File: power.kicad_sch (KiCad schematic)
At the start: 29 parts, among them U2 NCP691MN33T2G, U4 AP63301WU-7, U5 AP63301WU-7

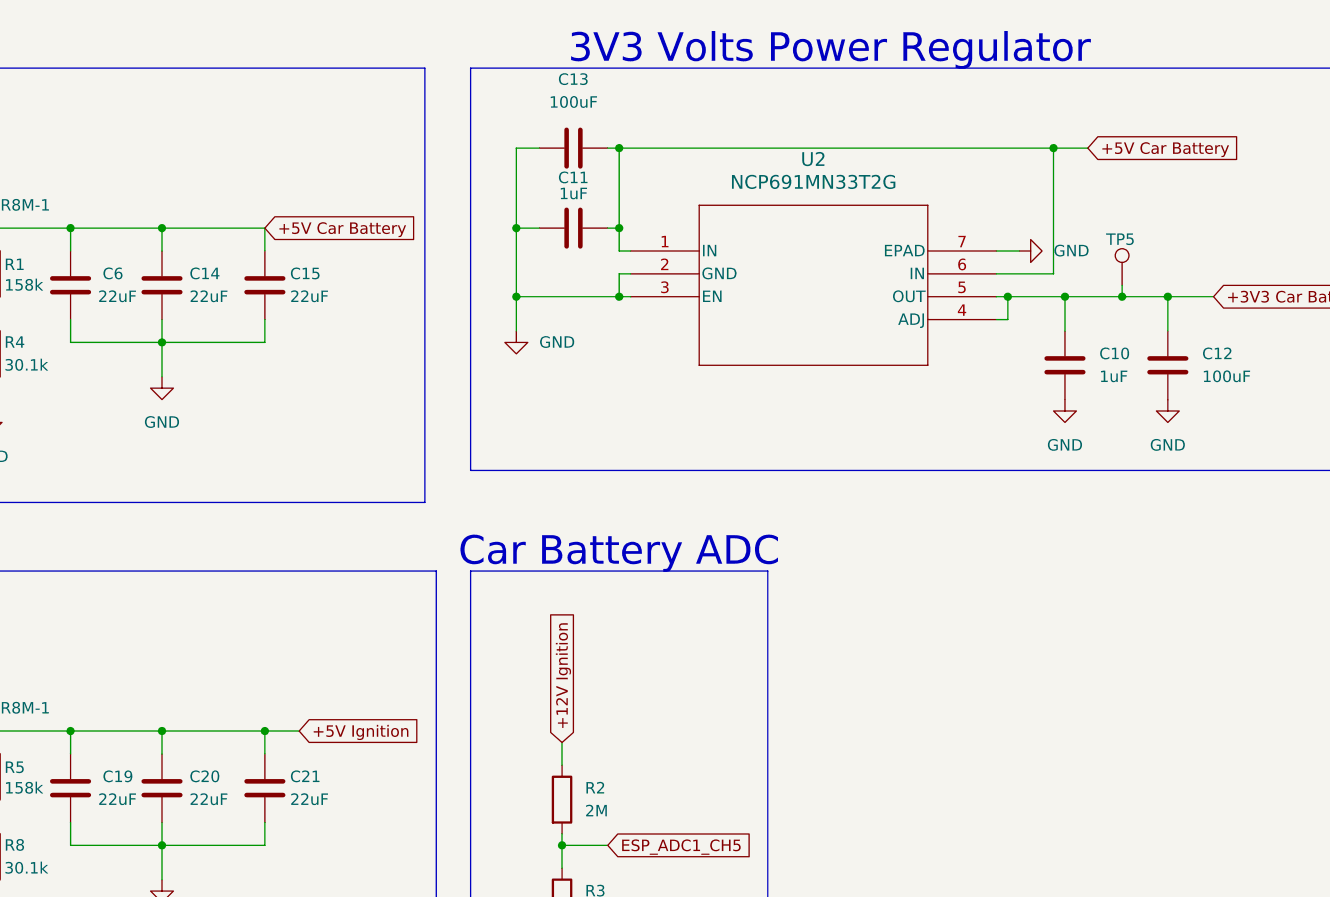
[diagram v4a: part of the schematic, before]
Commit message: added 3D models; light touch-ups
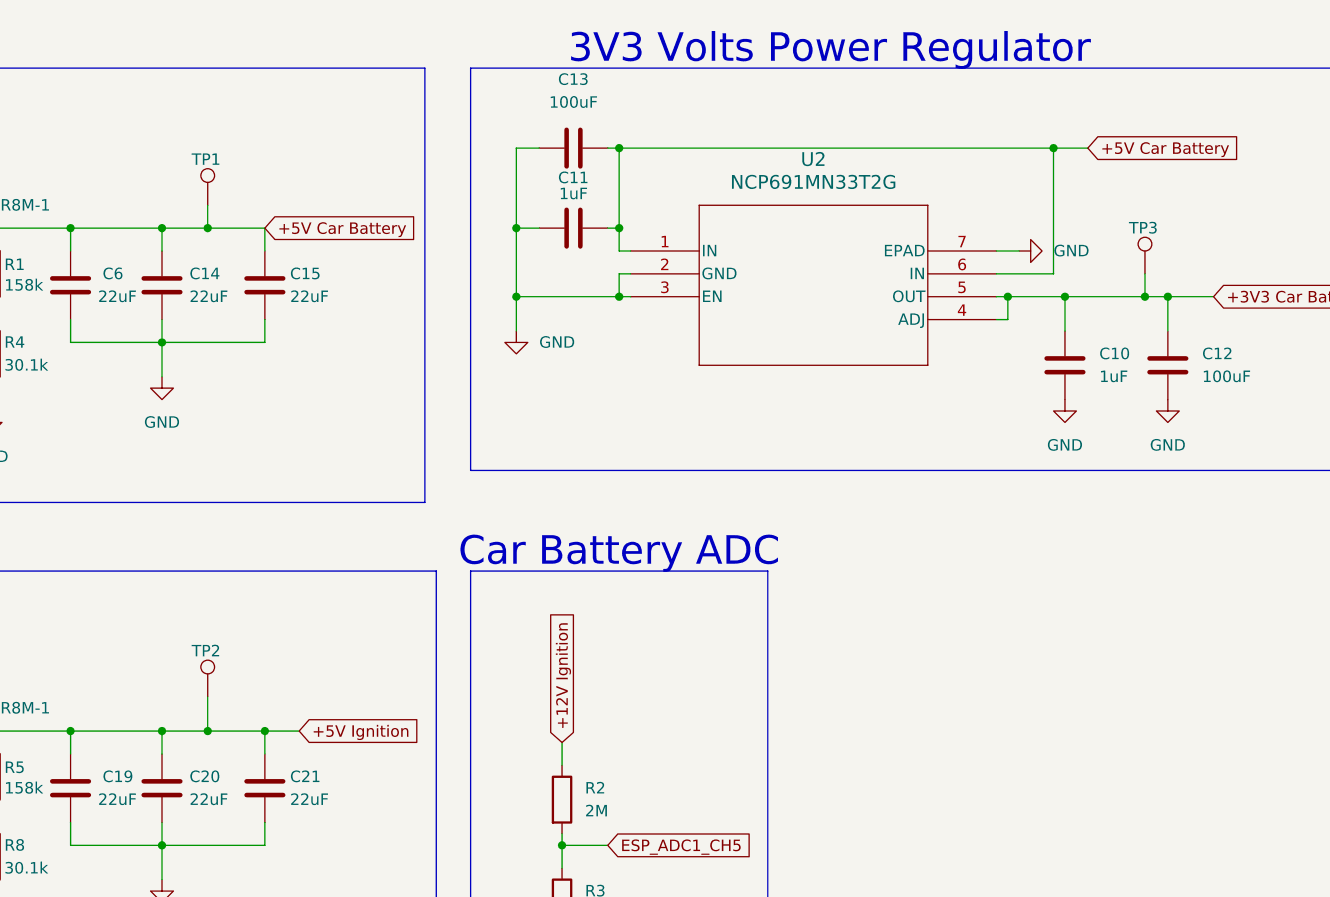
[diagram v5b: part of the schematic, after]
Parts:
- removed TP5: TestPoint, TestPoint:TestPoint_Pad_D1.0mm, symbol Connector:TestPoint
- added TP1, TP2, TP3: TestPoint, TestPoint:TestPoint_Pad_D1.0mm, symbol Connector:TestPoint
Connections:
- net +3V3 Car Battery: now also TP3.1
- net +5V Car Battery: now also TP1.1
- net +5V Ignition: now also TP2.1
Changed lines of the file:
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@@
 	)
 	(junction
+		(at 143.51 90.17)
+		(diameter 0)
+		(color 0 0 0 0)
+	)
+	(junction
 		(at 53.34 25.4)
 		(diameter 0)
@@
 	)
 	(junction
-		(at 245.11 41.91)
+		(at 247.65 41.91)
 		(diameter 0)
 		(color 0 0 0 0)
@@
 	)
 	(junction
+		(at 143.51 34.29)
+		(diameter 0)
+		(color 0 0 0 0)
+	)
+	(junction
 		(at 96.52 34.29)
 		(diameter 0)
@@
 	(wire
 		(pts
-			(xy 245.11 41.91) (xy 250.19 41.91)
+			(xy 238.76 41.91) (xy 247.65 41.91)
 		)
 		(stroke
@@
 	(wire
 		(pts
-			(xy 238.76 41.91) (xy 245.11 41.91)
+			(xy 119.38 99.06) (xy 119.38 100.33)
 		)
 		(stroke
@@
 	(wire
 		(pts
-			(xy 119.38 99.06) (xy 119.38 100.33)
+			(xy 53.34 81.28) (xy 43.18 81.28)
 		)
 		(stroke
@@
 	(wire
 		(pts
-			(xy 53.34 81.28) (xy 43.18 81.28)
+			(xy 149.86 44.45) (xy 149.86 46.99)
 		)
 		(stroke
@@
 	(wire
 		(pts
-			(xy 149.86 44.45) (xy 149.86 46.99)
+			(xy 231.14 44.45) (xy 232.41 44.45)
 		)
 		(stroke
@@
 	(wire
 		(pts
-			(xy 231.14 44.45) (xy 232.41 44.45)
+			(xy 247.65 41.91) (xy 250.19 41.91)
 		)
 		(stroke
@@
 	(wire
 		(pts
-			(xy 149.86 34.29) (xy 138.43 34.29)
+			(xy 149.86 34.29) (xy 143.51 34.29)
 		)
 		(stroke
@@
 	(wire
 		(pts
+			(xy 143.51 90.17) (xy 138.43 90.17)
+		)
+		(stroke
+			(width 0)
+			(type default)
+		)
+	)
+	(wire
+		(pts
 			(xy 232.41 44.45) (xy 232.41 41.91)
 		)
@@
 	(wire
 		(pts
-			(xy 149.86 90.17) (xy 138.43 90.17)
+			(xy 149.86 90.17) (xy 143.51 90.17)
 		)
 		(stroke
@@
 	(wire
 		(pts
+			(xy 143.51 86.36) (xy 143.51 90.17)
+		)
+		(stroke
+			(width 0)
+			(type default)
+		)
+	)
+	(wire
+		(pts
 			(xy 189.23 25.4) (xy 189.23 34.29)
 		)
@@
 	(wire
 		(pts
+			(xy 247.65 39.37) (xy 247.65 41.91)
+		)
+		(stroke
+			(width 0)
+			(type default)
+		)
+	)
+	(wire
+		(pts
 			(xy 138.43 102.87) (xy 149.86 102.87)
 		)
@@
 	(wire
 		(pts
-			(xy 245.11 40.64) (xy 245.11 41.91)
+			(xy 143.51 34.29) (xy 138.43 34.29)
+		)
+		(stroke
+			(width 0)
+			(type default)
+		)
+	)
+	(wire
+		(pts
+			(xy 143.51 31.75) (xy 143.51 34.29)
 		)
 		(stroke
@@
 	)
 	(symbol
-		(lib_id "Connector:TestPoint")
-		(at 245.11 40.64 0)
-		(unit 1)
-		(exclude_from_sim no)
-		(in_bom yes)
-		(on_board yes)
-		(dnp no)
-		(property "Reference" "TP5"
-			(at 243.332 35.56 0)
-			(effects
-				(font
-					(size 1.27 1.27)
-				)
-				(justify left)
-			)
-		)
-		(property "Value" "TestPoint"
-			(at 242.316 35.306 0)
-			(effects
-				(font
-					(size 1.27 1.27)
-				)
-				(justify left)
-				(hide yes)
-			)
-		)
-		(property "Footprint" "TestPoint:TestPoint_Pad_D1.0mm"
-			(at 250.19 40.64 0)
-			(effects
-				(font
-					(size 1.27 1.27)
-				)
-				(hide yes)
-			)
-		)
-		(property "Datasheet" "~"
-			(at 250.19 40.64 0)
-			(effects
-				(font
-					(size 1.27 1.27)
-				)
-				(hide yes)
-			)
-		)
-		(property "Description" "test point"
-			(at 245.11 40.64 0)
-			(effects
-				(font
-					(size 1.27 1.27)
-				)
-				(hide yes)
-			)
-		)
-		(pin "1"
-		)
-		(instances
-			(project "power"
-				(path "/0794a8bf-8b4d-4965-84ee-8314ec5cc547"
-					(reference "TP?")
-					(unit 1)
-				)
-			)
-			(project "main"
-				(path "/3ec17d1d-183f-42c7-9d9d-808fb8c0b5df/d298b733-9a46-47ce-8c62-0344f0cec928"
-					(reference "TP5")
-					(unit 1)
-				)
-			)
-		)
-	)
-	(symbol
 		(lib_id "power:GND")
 		(at 48.26 99.06 0)
@@
 	)
 	(symbol
+		(lib_id "Connector:TestPoint")
+		(at 143.51 31.75 0)
+		(unit 1)
+		(exclude_from_sim no)
+		(in_bom yes)
+		(on_board yes)
+		(dnp no)
+		(property "Reference" "TP1"
+			(at 141.732 26.67 0)
+			(effects
+				(font
+					(size 1.27 1.27)
+				)
+				(justify left)
+			)
+		)
+		(property "Value" "TestPoint"
+			(at 140.716 26.416 0)
+			(effects
+				(font
+					(size 1.27 1.27)
+				)
+				(justify left)
+				(hide yes)
+			)
+		)
+		(property "Footprint" "TestPoint:TestPoint_Pad_D1.0mm"
+			(at 148.59 31.75 0)
+			(effects
+				(font
+					(size 1.27 1.27)
+				)
+				(hide yes)
+			)
+		)
+		(property "Datasheet" "~"
+			(at 148.59 31.75 0)
+			(effects
+				(font
+					(size 1.27 1.27)
+				)
+				(hide yes)
+			)
+		)
+		(property "Description" "test point"
+			(at 143.51 31.75 0)
+			(effects
+				(font
+					(size 1.27 1.27)
+				)
+				(hide yes)
+			)
+		)
+		(pin "1"
+		)
+		(instances
+			(project "main"
+				(path "/3ec17d1d-183f-42c7-9d9d-808fb8c0b5df/d298b733-9a46-47ce-8c62-0344f0cec928"
+					(reference "TP1")
+					(unit 1)
+				)
+			)
+		)
+	)
+	(symbol
 		(lib_id "Device:C")
 		(at 43.18 87.63 0)
@@
 	)
 	(symbol
+		(lib_id "Connector:TestPoint")
+		(at 143.51 86.36 0)
+		(unit 1)
+		(exclude_from_sim no)
+		(in_bom yes)
+		(on_board yes)
+		(dnp no)
+		(property "Reference" "TP2"
+			(at 141.732 81.28 0)
+			(effects
+				(font
+					(size 1.27 1.27)
+				)
+				(justify left)
+			)
+		)
+		(property "Value" "TestPoint"
+			(at 140.716 81.026 0)
+			(effects
+				(font
+					(size 1.27 1.27)
+				)
+				(justify left)
+				(hide yes)
+			)
+		)
+		(property "Footprint" "TestPoint:TestPoint_Pad_D1.0mm"
+			(at 148.59 86.36 0)
+			(effects
+				(font
+					(size 1.27 1.27)
+				)
+				(hide yes)
+			)
+		)
+		(property "Datasheet" "~"
+			(at 148.59 86.36 0)
+			(effects
+				(font
+					(size 1.27 1.27)
+				)
+				(hide yes)
+			)
+		)
+		(property "Description" "test point"
+			(at 143.51 86.36 0)
+			(effects
+				(font
+					(size 1.27 1.27)
+				)
+				(hide yes)
+			)
+		)
+		(pin "1"
+		)
+		(instances
+			(project "main"
+				(path "/3ec17d1d-183f-42c7-9d9d-808fb8c0b5df/d298b733-9a46-47ce-8c62-0344f0cec928"
+					(reference "TP2")
+					(unit 1)
+				)
+			)
+		)
+	)
+	(symbol
 		(lib_id "Device:C")
 		(at 184.15 25.4 270)
@@
 					(unit 1)
 				)
+			)
+		)
+	)
+	(symbol
+		(lib_id "Connector:TestPoint")
+		(at 247.65 39.37 0)
+		(unit 1)
+		(exclude_from_sim no)
+		(in_bom yes)
+		(on_board yes)
+		(dnp no)
+		(property "Reference" "TP3"
+			(at 245.872 34.29 0)
+			(effects
+				(font
+					(size 1.27 1.27)
+				)
+				(justify left)
+			)
+		)
+		(property "Value" "TestPoint"
+			(at 244.856 34.036 0)
+			(effects
+				(font
+					(size 1.27 1.27)
+				)
+				(justify left)
+				(hide yes)
+			)
+		)
+		(property "Footprint" "TestPoint:TestPoint_Pad_D1.0mm"
+			(at 252.73 39.37 0)
+			(effects
+				(font
+					(size 1.27 1.27)
+				)
+				(hide yes)
+			)
+		)
+		(property "Datasheet" "~"
+			(at 252.73 39.37 0)
+			(effects
+				(font
+					(size 1.27 1.27)
+				)
+				(hide yes)
+			)
+		)
+		(property "Description" "test point"
+			(at 247.65 39.37 0)
+			(effects
+				(font
+					(size 1.27 1.27)
+				)
+				(hide yes)
+			)
+		)
+		(pin "1"
+		)
+		(instances
+			(project "main"
+				(path "/3ec17d1d-183f-42c7-9d9d-808fb8c0b5df/d298b733-9a46-47ce-8c62-0344f0cec928"
+					(reference "TP3")
+					(unit 1)
+				)

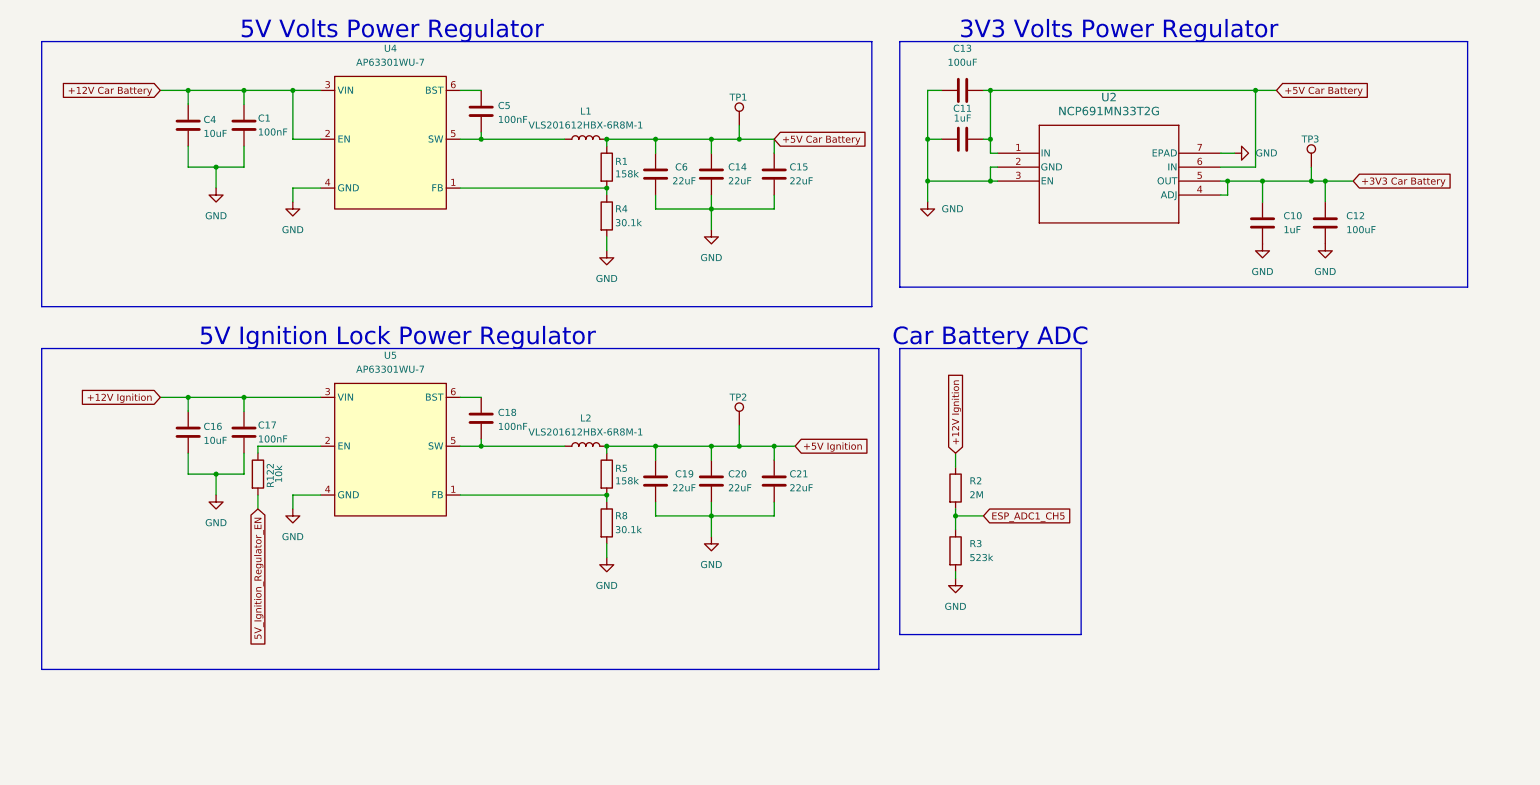
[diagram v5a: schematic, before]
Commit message: added tvs diodes, 100nF, pull-up for TSS interrupt
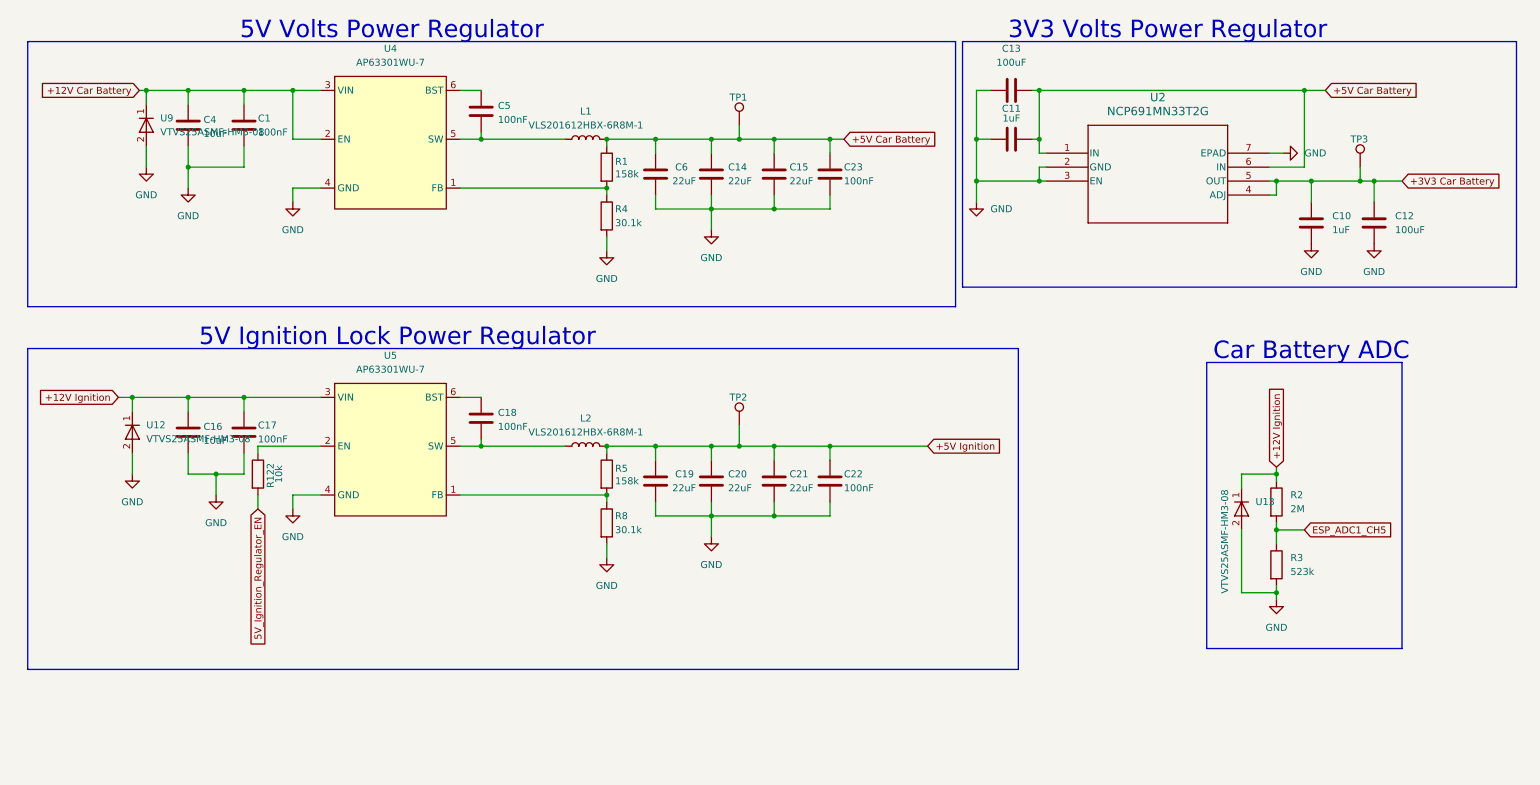
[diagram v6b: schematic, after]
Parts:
- added C22, C23: 100nF, Capacitor_SMD:C_0805_2012Metric, symbol Device:C
- added U12, U13, U9: VTVS25ASMF-HM3-08, Diode_SMD:D_SMF, symbol infotainment:VTVS25ASMF-HM3-08_
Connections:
- net +12V Car Battery: now also U9.1
- net +12V Ignition: now also U12.1, U13.1
- net +5V Car Battery: now also C23.1
- net +5V Ignition: now also C22.1
- net GND: now also C22.2, C23.2, U12.2, U13.2, U9.2
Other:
- moved on the sheet: C10, C11, C12, C13, R2, R3, TP3, U2

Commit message: Modified ADC resistors. Added bypass cap to ADC.
Removed some ground islands.
Removed lock files and added them to gitignore.
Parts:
- added C24: 100nF, Capacitor_SMD:C_0805_2012Metric, symbol Device:C
- R2: value 2M -> 90k
- R3: value 523k -> 10k
- renumbered TP3 to 3V3_B1, TP1 to 5V_B1, TP2 to 5V_I1
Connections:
- net ESP_ADC1_CH5: now also C24.1
- net GND: now also C24.2
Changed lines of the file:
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@@
 	)
 	(junction
+		(at 252.73 105.41)
+		(diameter 0)
+		(color 0 0 0 0)
+	)
+	(junction
 		(at 259.08 41.91)
 		(diameter 0)
@@
 	(wire
 		(pts
+			(xy 252.73 105.41) (xy 260.35 105.41)
+		)
+		(stroke
+			(width 0)
+			(type default)
+		)
+	)
+	(wire
+		(pts
 			(xy 196.85 25.4) (xy 198.12 25.4)
 		)
@@
 	(wire
 		(pts
+			(xy 252.73 114.3) (xy 252.73 116.84)
+		)
+		(stroke
+			(width 0)
+			(type default)
+		)
+	)
+	(wire
+		(pts
 			(xy 246.38 25.4) (xy 246.38 39.37)
 		)
@@
 	(wire
 		(pts
-			(xy 241.3 105.41) (xy 246.38 105.41)
+			(xy 241.3 105.41) (xy 252.73 105.41)
 		)
 		(stroke
@@
 	(wire
 		(pts
+			(xy 252.73 106.68) (xy 252.73 105.41)
+		)
+		(stroke
+			(width 0)
+			(type default)
+		)
+	)
+	(wire
+		(pts
 			(xy 62.23 34.29) (xy 62.23 25.4)
 		)
@@
 	(wire
 		(pts
+			(xy 252.73 116.84) (xy 241.3 116.84)
+		)
+		(stroke
+			(width 0)
+			(type default)
+		)
+	)
+	(wire
+		(pts
 			(xy 53.34 83.82) (xy 53.34 81.28)
 		)
@@
 	(global_label "ESP_ADC1_CH5"
 		(shape input)
-		(at 246.38 105.41 0)
+		(at 260.35 105.41 0)
 		(fields_autoplaced yes)
 		(effects
@@
 		)
 		(property "Intersheetrefs" "${INTERSHEET_REFS}"
-			(at 263.577 105.41 0)
+			(at 277.547 105.41 0)
 			(effects
 				(font
@@
 			)
 		)
-		(property "Value" "2M"
+		(property "Value" "90k"
 			(at 243.84 101.5999 0)
 			(effects
@@
 		(on_board yes)
 		(dnp no)
-		(property "Reference" "TP1"
+		(property "Reference" "5V_B1"
 			(at 141.732 26.67 0)
 			(effects
@@
 			(project "main"
 				(path "/3ec17d1d-183f-42c7-9d9d-808fb8c0b5df/d298b733-9a46-47ce-8c62-0344f0cec928"
-					(reference "TP1")
+					(reference "5V_B1")
 					(unit 1)
 				)
@@
 			)
 		)
-		(property "Value" "523k"
+		(property "Value" "10k"
 			(at 243.84 113.0299 0)
 			(effects
@@
 		(on_board yes)
 		(dnp no)
-		(property "Reference" "TP2"
+		(property "Reference" "5V_I1"
 			(at 141.732 81.28 0)
 			(effects
@@
 			(project "main"
 				(path "/3ec17d1d-183f-42c7-9d9d-808fb8c0b5df/d298b733-9a46-47ce-8c62-0344f0cec928"
-					(reference "TP2")
+					(reference "5V_I1")
 					(unit 1)
 				)
@@
 	)
 	(symbol
+		(lib_id "Device:C")
+		(at 252.73 110.49 0)
+		(unit 1)
+		(exclude_from_sim no)
+		(in_bom yes)
+		(on_board yes)
+		(dnp no)
+		(property "Reference" "C24"
+			(at 255.27 109.22 0)
+			(effects
+				(font
+					(size 1.27 1.27)
+				)
+				(justify left)
+			)
+		)
+		(property "Value" "100nF"
+			(at 255.27 111.76 0)
+			(effects
+				(font
+					(size 1.27 1.27)
+				)
+				(justify left)
+			)
+		)
+		(property "Footprint" "Capacitor_SMD:C_0805_2012Metric"
+			(at 253.6952 114.3 0)
+			(effects
+				(font
+					(size 1.27 1.27)
+				)
+				(hide yes)
+			)
+		)
+		(property "Datasheet" "~"
+			(at 252.73 110.49 0)
+			(effects
+				(font
+					(size 1.27 1.27)
+				)
+				(hide yes)
+			)
+		)
+		(property "Description" "Unpolarized capacitor"
+			(at 252.73 110.49 0)
+			(effects
+				(font
+					(size 1.27 1.27)
+				)
+				(hide yes)
+			)
+		)
+		(pin "1"
+		)
+		(pin "2"
+		)
+		(instances
+			(project "main"
+				(path "/3ec17d1d-183f-42c7-9d9d-808fb8c0b5df/d298b733-9a46-47ce-8c62-0344f0cec928"
+					(reference "C24")
+					(unit 1)
+				)
+			)
+		)
+	)
+	(symbol
 		(lib_id "power:GND")
 		(at 247.65 53.34 0)
@@
 		(on_board yes)
 		(dnp no)
-		(property "Reference" "TP3"
+		(property "Reference" "3V3_B1"
 			(at 254.762 34.29 0)
 			(effects
@@
 			(project "main"
 				(path "/3ec17d1d-183f-42c7-9d9d-808fb8c0b5df/d298b733-9a46-47ce-8c62-0344f0cec928"
-					(reference "TP3")
+					(reference "3V3_B1")
 					(unit 1)
 				)

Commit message: Change inductor type.
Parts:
- L1, L2: value VLS201612HBX-6R8M-1 -> 4.7uH; footprint Inductor_SMD:L_Cenker_CKCS201610 -> footprints:IND_TYA40204_LRD
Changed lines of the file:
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@@
 			)
 		)
-		(property "Value" "VLS201612HBX-6R8M-1"
+		(property "Value" "4.7uH"
 			(at 115.57 31.75 90)
 			(effects
@@
 			)
 		)
-		(property "Footprint" "Inductor_SMD:L_Cenker_CKCS201610"
+		(property "Footprint" "footprints:IND_TYA40204_LRD"
 			(at 115.57 34.29 0)
 			(effects
@@
 			)
 		)
-		(property "Description" "Inductor - 6.8uH"
+		(property "Description" "Inductor"
 			(at 115.57 34.29 0)
 			(effects
@@
 	)
 	(symbol
-		(lib_name "VTVS25ASMF-HM3-08__1")
 		(lib_id "infotainment:VTVS25ASMF-HM3-08_")
 		(at 35.56 31.75 270)
@@
 			)
 		)
-		(property "Value" "VLS201612HBX-6R8M-1"
+		(property "Value" "4.7uH"
 			(at 115.57 87.63 90)
 			(effects
@@
 			)
 		)
-		(property "Footprint" "Inductor_SMD:L_Cenker_CKCS201610"
+		(property "Footprint" "footprints:IND_TYA40204_LRD"
 			(at 115.57 90.17 0)
 			(effects
@@
 			)
 		)
-		(property "Description" "Inductor - 6.8uH"
+		(property "Description" "Inductor"
 			(at 115.57 90.17 0)
 			(effects
@@
 	)
 	(symbol
-		(lib_name "ap63301wu-7_1")
 		(lib_id "infotainment:ap63301wu-7")
 		(at 80.01 43.18 0)
@@
 	)
 	(symbol
-		(lib_name "VTVS25ASMF-HM3-08__2")
 		(lib_id "infotainment:VTVS25ASMF-HM3-08_")
 		(at 33.02 87.63 270)
